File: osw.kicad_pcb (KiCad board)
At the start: 4 copper layers, 45 x 41 mm, 0 parts

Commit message: Finished schematic.  Ready to begin board layout.
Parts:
- added C1: cap0402_1p0u10V, open-Smartwatch:C_0402_1005Metric_osw, F.Cu at (245.0, 112.0)
- added C10: cap0402_4p7u10V, open-Smartwatch:C_0402_1005Metric_osw, F.Cu at (255.4, 100.5)
- added C11: cap0402_4p7u10V, open-Smartwatch:C_0402_1005Metric_osw, F.Cu at (239.5, 117.9)
- added C12: 1u, open-Smartwatch:C_0402_1005Metric_osw, F.Cu at (249.7, 107.4)
- added C13: cap0402_p1u10V, open-Smartwatch:C_0402_1005Metric_osw, F.Cu at (236.6, 120.4)
- added C14: cap0402_p1u10V, open-Smartwatch:C_0402_1005Metric_osw, F.Cu at (229.4, 128.9)
- added C15: cap0402_p1u10V, open-Smartwatch:C_0402_1005Metric_osw, F.Cu at (234.6, 123.1)
- added C16: cap0402_p1u10V, open-Smartwatch:C_0402_1005Metric_osw, F.Cu at (263.2, 95.1)
- added C17: cap0402_1p0u10V, open-Smartwatch:C_0402_1005Metric_osw, F.Cu at (266.1, 91.2)
- added C18: cap0402_1p0u10V, open-Smartwatch:C_0402_1005Metric_osw, F.Cu at (250.3, 105.4)
- added C2: cap0402_p1u10V, open-Smartwatch:C_0402_1005Metric_osw, F.Cu at (263.2, 93.1)
- added C3: cap0402_4p7u10V, open-Smartwatch:C_0402_1005Metric_osw, F.Cu at (246.8, 109.6)
- added C4: cap0402_4p7u10V, open-Smartwatch:C_0402_1005Metric_osw, F.Cu at (260.1, 97.1)
- added C5: cap0402_p1u10V, open-Smartwatch:C_0402_1005Metric_osw, F.Cu at (232.3, 125.1)
- added C6: cap0402_p1u10V, open-Smartwatch:C_0402_1005Metric_osw, F.Cu at (266.1, 93.1)
- added C7: cap0402_p1u10V, open-Smartwatch:C_0402_1005Metric_osw, F.Cu at (226.5, 130.9)
- added C8: cap0402_p1u10V, open-Smartwatch:C_0402_1005Metric_osw, F.Cu at (253.2, 102.5)
- added C9: cap0402_p1u10V, open-Smartwatch:C_0402_1005Metric_osw, F.Cu at (253.2, 104.5)
- added D1: LED_redSMD, open-Smartwatch:Harvatek_LED_osw, F.Cu at (249.3, 109.5)
- added J1: Conn_01x02, Connector_PinHeader_2.54mm:PinHeader_1x02_P2.54mm_Vertical, F.Cu at (248.8, 97.6)
- added J2: microSD_MEM2067-02-180-00-A_REVB, open-Smartwatch:GCT_MEM2067-02-180-00-A_REVB, F.Cu at (201.6, 123.0)
- added J3: usbc_USB4056-03-A, open-Smartwatch:GCT_USB4056-03-A_REVA, F.Cu at (239.9, 98.9)
- added Q1: Q_NMOS_ToshibaSMD, open-Smartwatch:SOT95P247X115-3N, F.Cu at (243.6, 104.4)
- added R1: res0402_470, open-Smartwatch:R_0402_1005Metric_osw, F.Cu at (260.3, 93.2)
- added R10: res0402_10k, open-Smartwatch:R_0402_1005Metric_osw, F.Cu at (223.6, 131.5)
- added R11: res0402_10k, open-Smartwatch:R_0402_1005Metric_osw, F.Cu at (250.4, 103.5)
- added R12: res0402_1k, open-Smartwatch:R_0402_1005Metric_osw, F.Cu at (226.5, 128.9)
- added R13: res0402_10k, open-Smartwatch:R_0402_1005Metric_osw, F.Cu at (242.1, 114.0)
- added R14: res0402_56k, open-Smartwatch:R_0402_1005Metric_osw, F.Cu at (257.3, 95.5)
- added R15: res0402_0, open-Smartwatch:R_0402_1005Metric_osw, F.Cu at (246.8, 107.7)
- added R16: res0402_10k, open-Smartwatch:R_0402_1005Metric_osw, F.Cu at (260.3, 91.2)
- added R17: res0402_10k, open-Smartwatch:R_0402_1005Metric_osw, F.Cu at (229.4, 127.0)
- added R18: res0402_5p6k, open-Smartwatch:R_0402_1005Metric_osw, F.Cu at (252.6, 100.5)
- added R19: res0402_470, open-Smartwatch:R_0402_1005Metric_osw, F.Cu at (247.4, 103.5)
- added R2: res0402_1k, open-Smartwatch:R_0402_1005Metric_osw, F.Cu at (257.3, 97.5)
- added R20: res0402_10k, open-Smartwatch:R_0402_1005Metric_osw, F.Cu at (236.6, 118.5)
- added R21: res0402_10k, open-Smartwatch:R_0402_1005Metric_osw, F.Cu at (242.1, 112.0)
- added R3: res0402_1k, open-Smartwatch:R_0402_1005Metric_osw, F.Cu at (247.4, 105.5)
- added R4: res0402_10k, open-Smartwatch:R_0402_1005Metric_osw, F.Cu at (239.0, 115.9)
- added R5: res0402_1k, open-Smartwatch:R_0402_1005Metric_osw, F.Cu at (231.8, 123.1)
- added R6: res0402_10k, open-Smartwatch:R_0402_1005Metric_osw, F.Cu at (263.2, 91.2)
- added R7: res0402_10k, open-Smartwatch:R_0402_1005Metric_osw, F.Cu at (260.3, 95.1)
- added R8: res0402_10k, open-Smartwatch:R_0402_1005Metric_osw, F.Cu at (226.5, 127.0)
- added R9: res0402_10k, open-Smartwatch:R_0402_1005Metric_osw, F.Cu at (220.7, 131.5)
- added SW1: SPST_EVQ-P7J01P, open-Smartwatch:SW_EVQ-P7J01P, F.Cu at (237.3, 109.5)
- added SW2: SPST_EVQ-P7J01P, open-Smartwatch:SW_EVQ-P7J01P, F.Cu at (237.3, 104.4)
- added SW3: SPST_EVQ-P7J01P, open-Smartwatch:SW_EVQ-P7J01P, F.Cu at (250.4, 92.4)
- added SW4: SPST_EVQ-P7J01P, open-Smartwatch:SW_EVQ-P7J01P, F.Cu at (234.3, 114.6)
- added U1: L96-M33, open-Smartwatch:XCVR_L96-M33, F.Cu at (223.9, 101.8)
- added U10: BMA400, open-Smartwatch:LGA-12_2x2mm_P0.5mm, F.Cu at (211.8, 120.2)
- added U11: GC9A01_IPS_display_SPI, open-Smartwatch:GC9A01_IPS_display, F.Cu at (222.4, 123.6)
- added U12: esd_USB_IP4234CZ6, open-Smartwatch:SOT-457_ESD, F.Cu at (256.3, 92.3)
- added U13: BH1792GLC-E2, open-Smartwatch:XDCR_BH1792GLC-E2, F.Cu at (243.2, 108.8)
- added U2: TPS22933, open-Smartwatch:uqfn_1p5x1p5_8_tps22933, F.Cu at (212.3, 116.7)
- added U3: ESP32-S3-WROOM, open-Smartwatch:XCVR_ESP32-S3-WROOM-1U, F.Cu at (204.3, 104.1)
- added U4: MCP73831T-2ACI_OT, open-Smartwatch:SOT-23-5, F.Cu at (232.7, 119.8)
- added U5: MIC5504-3p3, open-Smartwatch:VREG_MIC5504-3.3YMT-TZ, F.Cu at (239.2, 113.6)
- added U6: FT234XD-R, open-Smartwatch:SON45P300X300X80-13N, F.Cu at (222.4, 128.2)
- added U7: MIC5504-3p3, open-Smartwatch:VREG_MIC5504-3.3YMT-TZ, F.Cu at (211.7, 123.2)
- added U8: 23K256-I/SN, open-Smartwatch:SOIC127P600X175-8N_microchipRAM, F.Cu at (215.1, 129.2)
- added U9: PCF85063ATL/1,118, open-Smartwatch:10-DFN(2.6X2.6)_PCF85063A, F.Cu at (253.7, 97.4)

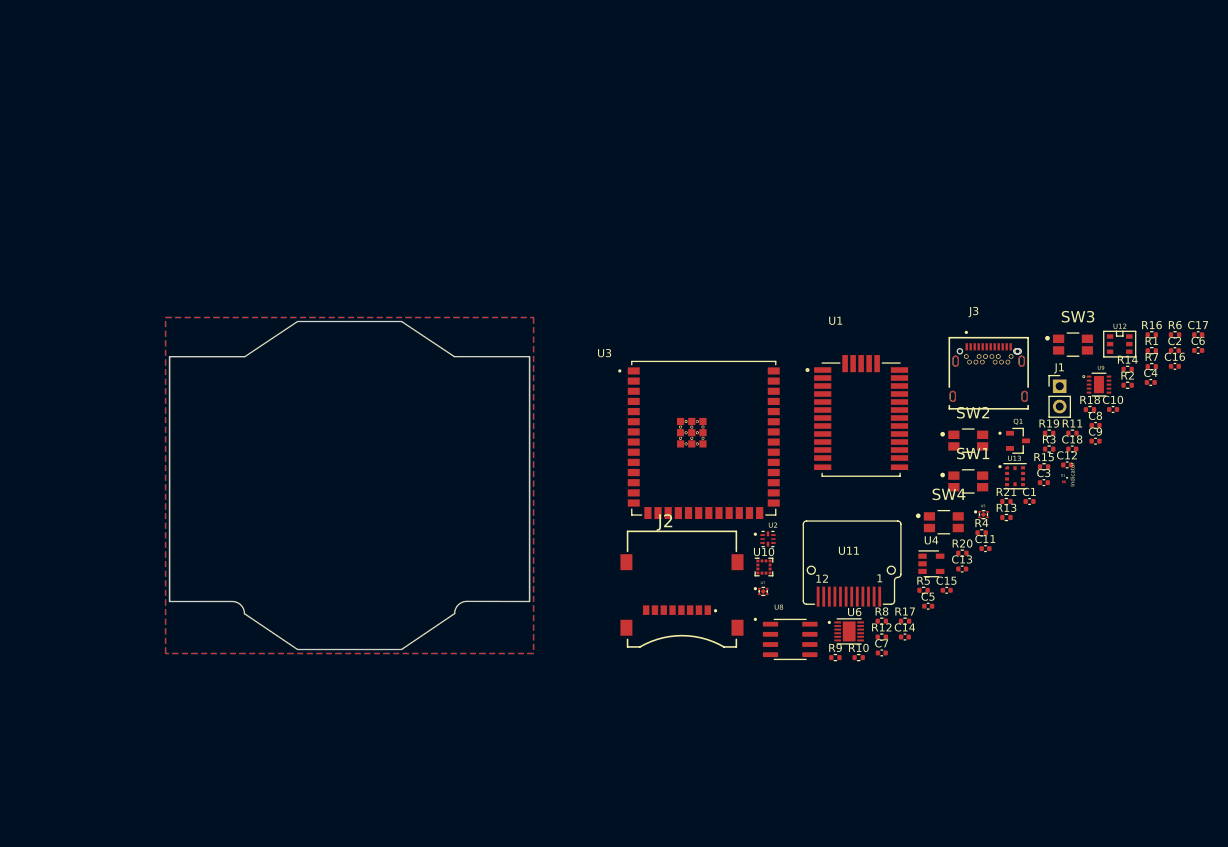
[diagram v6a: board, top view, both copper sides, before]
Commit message: Updating the docs for the schematic.  May need to swap out the ESP chip as it is quite wide for the board layout....
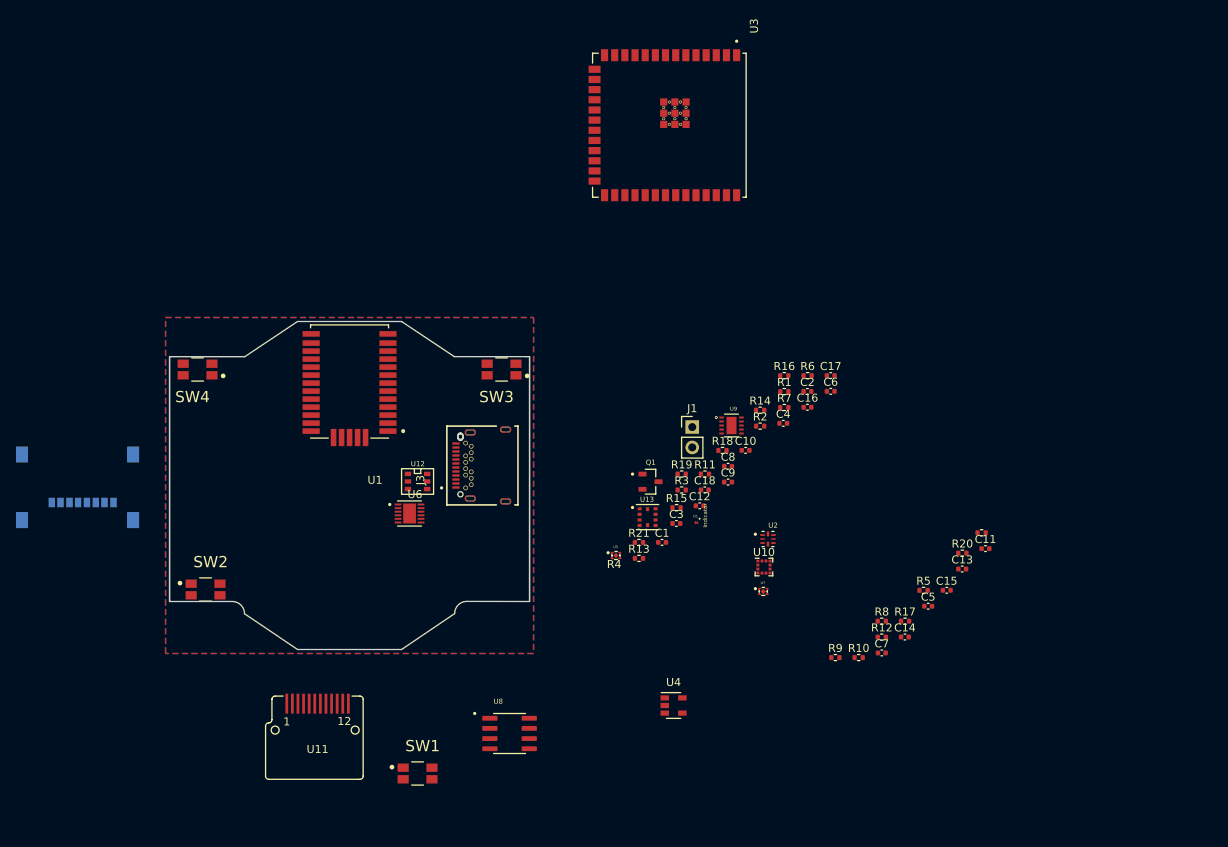
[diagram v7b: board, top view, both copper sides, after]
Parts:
- J2: moved to B.Cu
- moved SW2 97.1 mm to (142.0, 123.0)
- moved SW4 95.2 mm to (141.0, 95.5), turned to 180 degrees
- moved U12 89.4 mm to (168.5, 109.5)
- moved SW1 77.9 mm to (168.5, 146.0)
- moved J2 76.7 mm to (126.0, 109.5), turned to 180 degrees
- moved SW3 71.5 mm to (179.0, 95.5), turned to 180 degrees
- moved U11 67.9 mm to (156.0, 137.5), turned to 180 degrees
- moved U1 64.1 mm to (160.0, 97.0), turned to 180 degrees
- moved J3 61.0 mm to (179.5, 107.5), turned to 90 degrees
- moved U6 56.9 mm to (167.5, 113.5)
- moved C16 46.2 mm to (217.2, 100.2)
- moved C18 46.2 mm to (204.4, 110.5)
- moved C2 46.2 mm to (217.2, 98.2)
- moved J1 46.2 mm to (202.8, 102.7)
- moved Q1 46.2 mm to (197.6, 109.5)
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
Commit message: Updates to the schematic to use a smaller packaged ESP32.
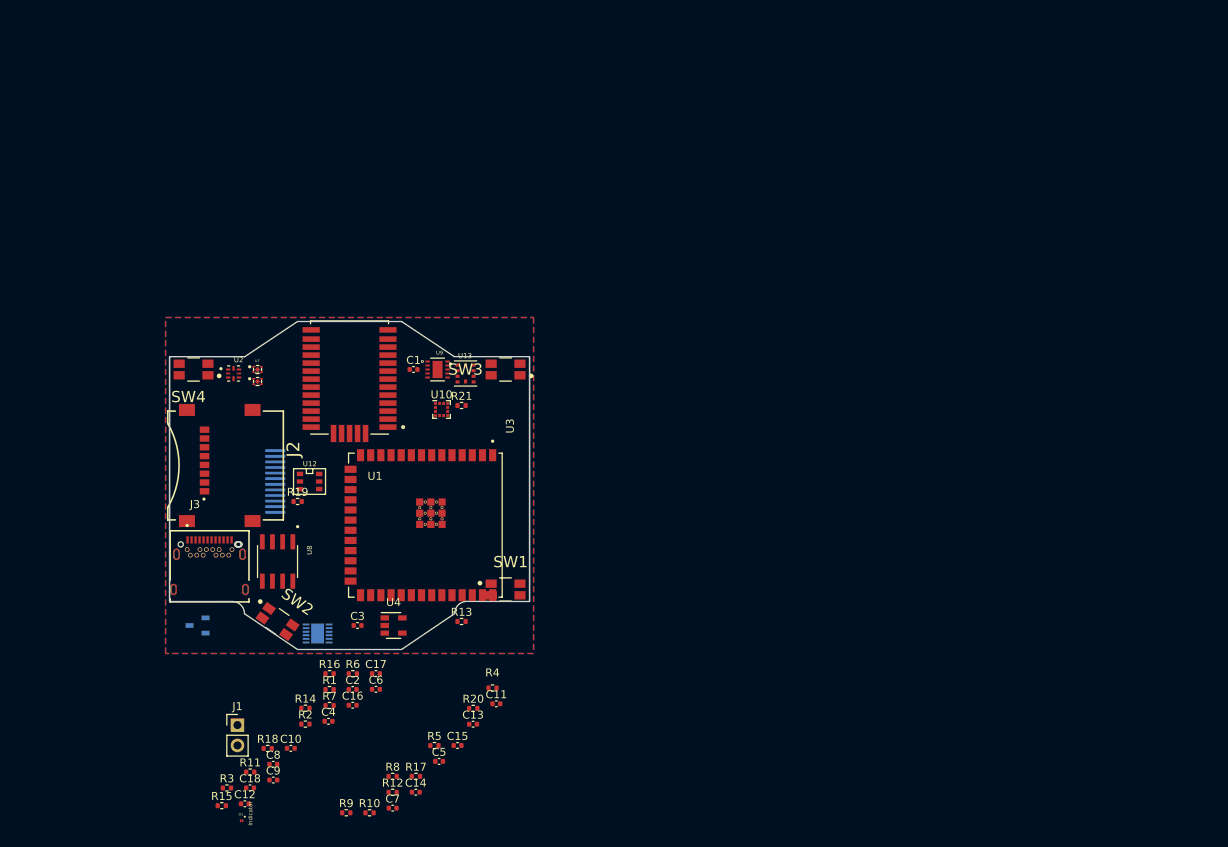
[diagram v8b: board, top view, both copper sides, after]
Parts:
- J2: moved to F.Cu
- Q1, U11, U6: moved to B.Cu
- moved U2 69.9 mm to (145.5, 96.0)
- moved U7 69.0 mm to (148.5, 95.5)
- moved C10 68.0 mm to (152.7, 142.9)
- moved C16 68.0 mm to (160.4, 137.5)
- moved C2 68.0 mm to (160.4, 135.5)
- moved C8 68.0 mm to (150.5, 144.8)
- moved C9 68.0 mm to (150.5, 146.8)
- moved D1 68.0 mm to (146.5, 151.9)
- moved R14 68.0 mm to (154.5, 137.8)
- moved R16 68.0 mm to (157.5, 133.5)
- moved R2 68.0 mm to (154.5, 139.8)
- moved R3 68.0 mm to (144.7, 147.8)
- moved R6 68.0 mm to (160.4, 133.5)
- moved R7 68.0 mm to (157.5, 137.5)
- moved C12 68.0 mm to (146.9, 149.8)
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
